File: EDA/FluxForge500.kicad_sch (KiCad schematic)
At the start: 0 parts

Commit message: Added more structure and added chosen power MOSFET
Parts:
- added Q1: SFG019N100C3, FluxForge500-lib:TO-247-4_L16.8-W5.0-L, symbol FluxForge500:SFG019N100C3
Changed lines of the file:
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@@
 	(generator_version "9.0")
 	(paper "A4")
+	(symbol
+		(lib_id "FluxForge500:SFG019N100C3")
+		(at 123.19 69.85 0)
+		(unit 1)
+		(exclude_from_sim no)
+		(in_bom yes)
+		(on_board yes)
+		(dnp no)
+		(fields_autoplaced yes)
+		(property "Reference" "Q1"
+			(at 130.81 69.8499 0)
+			(effects
+				(font
+					(size 1.27 1.27)
+				)
+				(justify left)
+			)
+		)
+		(property "Value" "SFG019N100C3"
+			(at 130.81 72.3899 0)
+			(effects
+				(font
+					(size 1.27 1.27)
+				)
+				(justify left)
+			)
+		)
+		(property "Footprint" "FluxForge500-lib:TO-247-4_L16.8-W5.0-L"
+			(at 123.19 82.55 0)
+			(effects
+				(font
+					(size 1.27 1.27)
+				)
+				(hide yes)
+			)
+		)
+		(property "Datasheet" "https://www.lcsc.com/datasheet/C49257109.pdf"
+			(at 123.19 85.09 0)
+			(effects
+				(font
+					(size 1.27 1.27)
+				)
+				(hide yes)
+			)
+		)
+		(property "Description" ""
+			(at 123.19 69.85 0)
+			(effects
+				(font
+					(size 1.27 1.27)
+				)
+				(hide yes)
+			)
+		)
+		(property "Manufacturer" "赛力康电气"
+			(at 123.19 87.63 0)
+			(effects
+				(font
+					(size 1.27 1.27)
+				)
+				(hide yes)
+			)
+		)
+		(property "MPN" "SFG019N100C3"
+			(at 123.19 90.17 0)
+			(effects
+				(font
+					(size 1.27 1.27)
+				)
+				(hide yes)
+			)
+		)
+		(property "LCSC Part" "C49257109"
+			(at 123.19 92.71 0)
+			(effects
+				(font
+					(size 1.27 1.27)
+				)
+				(hide yes)
+			)
+		)
+		(pin "3"
+		)
+		(pin "2"
+		)
+		(pin "1"
+		)
+		(pin "4"
+		)
+		(instances
+			(project ""
+				(path "/a2f35304-c637-43ce-ab88-fc8f2dc2eb48"
+					(reference "Q1")
+					(unit 1)
+				)
+			)
+		)
+	)
 	(sheet_instances
 		(path "/"

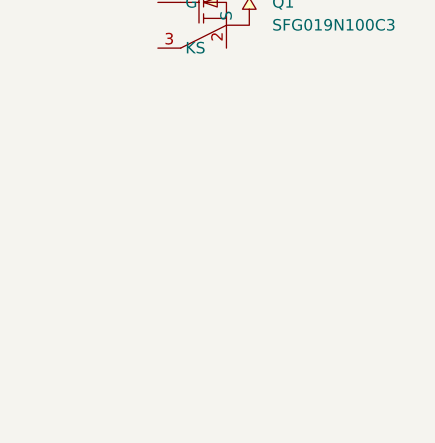
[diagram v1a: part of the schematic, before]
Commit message: Added chosen gate driver
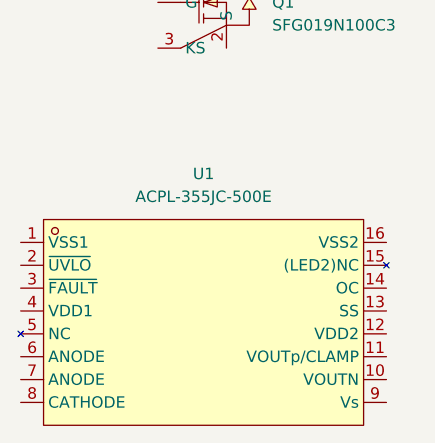
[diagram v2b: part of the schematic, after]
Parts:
- added U1: ACPL-355JC-500E, FluxForge500-lib:WSOIC-16_L10.3-W7.5-P1.27-LS10.3-BL, symbol FluxForge500:ACPL-355JC-500E
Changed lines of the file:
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@@
+		)
+	)
+	(symbol
+		(lib_id "FluxForge500:ACPL-355JC-500E")
+		(at 123.19 105.41 0)
+		(unit 1)
+		(exclude_from_sim no)
+		(in_bom yes)
+		(on_board yes)
+		(dnp no)
+		(fields_autoplaced yes)
+		(property "Reference" "U1"
+			(at 123.19 88.9 0)
+			(effects
+				(font
+					(size 1.27 1.27)
+				)
+			)
+		)
+		(property "Value" "ACPL-355JC-500E"
+			(at 123.19 91.44 0)
+			(effects
+				(font
+					(size 1.27 1.27)
+				)
+			)
+		)
+		(property "Footprint" "FluxForge500-lib:WSOIC-16_L10.3-W7.5-P1.27-LS10.3-BL"
+			(at 123.19 121.92 0)
+			(effects
+				(font
+					(size 1.27 1.27)
+				)
+				(hide yes)
+			)
+		)
+		(property "Datasheet" "https://www.lcsc.com/datasheet/C38013275.pdf"
+			(at 123.19 124.46 0)
+			(effects
+				(font
+					(size 1.27 1.27)
+				)
+				(hide yes)
+			)
+		)
+		(property "Description" ""
+			(at 123.19 105.41 0)
+			(effects
+				(font
+					(size 1.27 1.27)
+				)
+				(hide yes)
+			)
+		)
+		(property "Manufacturer" "Broadcom(博通)"
+			(at 123.19 127 0)
+			(effects
+				(font
+					(size 1.27 1.27)
+				)
+				(hide yes)
+			)
+		)
+		(property "MPN" "ACPL-355JC-500E"
+			(at 123.19 129.54 0)
+			(effects
+				(font
+					(size 1.27 1.27)
+				)
+				(hide yes)
+			)
+		)
+		(property "LCSC Part" "C38013275"
+			(at 123.19 132.08 0)
+			(effects
+				(font
+					(size 1.27 1.27)
+				)
+				(hide yes)
+			)
+		)
+		(pin "8"
+		)
+		(pin "6"
+		)
+		(pin "4"
+		)
+		(pin "13"
+		)
+		(pin "2"
+		)
+		(pin "3"
+		)
+		(pin "5"
+		)
+		(pin "7"
+		)
+		(pin "1"
+		)
+		(pin "16"
+		)
+		(pin "15"
+		)
+		(pin "14"
+		)
+		(pin "11"
+		)
+		(pin "10"
+		)
+		(pin "12"
+		)
+		(pin "9"
+		)
+		(instances
+			(project ""
+				(path "/a2f35304-c637-43ce-ab88-fc8f2dc2eb48"
+					(reference "U1")
+					(unit 1)
+				)
+			)
 		)
 	)

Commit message: Worked on schematic
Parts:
- removed U1: ACPL-355JC-500E, FluxForge500-lib:WSOIC-16_L10.3-W7.5-P1.27-LS10.3-BL, symbol FluxForge500:ACPL-355JC-500E
- added C1: 47pF, symbol Device:C
- added C10, C11, C7, C8, C9: 10uF, symbol Device:C
- added C12, C13: 180uF, symbol Device:C
- added C14: 1uF, symbol Device:C
- added C2, C3, C4, C5, C6: 4.7uF, symbol Device:C
- added L1: L, symbol Device:L
- added Q2, Q3, Q4: SFG019N100C3, FluxForge500-lib:TO-247-4_L16.8-W5.0-L, symbol FluxForge500:SFG019N100C3
- added R1, R2, R3, R4: 10Ω, symbol Device:R
- added R10, R6, R7, R9: 100Ω, symbol Device:R
- added R5: 8mΩ, symbol Device:R
- added R8: 0Ω, symbol Device:R
- added U1, U2, U3, U4: STGAP2SCMTR, FluxForge500-lib:SO-8_L4.9-W3.9-P1.27-LS5.9-BL, symbol FluxForge500:STGAP2SMTR
- added U5: LM5176PWPR, FluxForge500-lib:HTSSOP-28_L9.7-W4.4-P0.65-LS6.4-BL-EP, symbol FluxForge500:LM5176PWPR
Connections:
- net at Q1.1 (D): now also C2.1, C3.1, C4.1, C5.1, C6.1
- net at Q1.2 (S): now also L1.1, Q2.1 (D)
- net at Q1.3 (KS): now also U1.8 (GNDISO)
- net at Q1.4 (G): now also R1.2, U1.7 (CLAMP)
- new net: Q2.2 (S), Q4.2 (S), R5.1, R6.2
- new net: Q2.3 (KS), U2.8 (GNDISO)
- new net: Q2.4 (G), R2.2, U2.7 (CLAMP)
- new net: Q3.4 (G), R3.1, U3.7 (CLAMP)
- new net: R3.2, U3.6 (GOUT)
- new net: C10.1, C11.1, C7.1, C8.1, C9.1, Q3.1 (D), R10.2, R8.1
- new net: R1.1, U1.6 (GOUT)
- new net: R2.1, U2.6 (GOUT)
- new net: L1.2, Q3.2 (S), Q4.1 (D)
- new net: Q4.4 (G), R4.1, U4.7 (CLAMP)
- new net: R4.2, U4.6 (GOUT)
- new net: Q3.3 (KS), U3.8 (GNDISO)
- new net: C12.2, C13.2
- new net: Q4.3 (KS), U4.8 (GNDISO)
- new net CS: C1.1, R6.1, U5.16 (CS)
- new net CSG: C1.2, R7.1, U5.15 (CSG)
- new net GND: C10.2, C11.2, C2.2, C3.2, C4.2, C5.2, C6.2, C7.2, C8.2, C9.2, R5.2, R7.2
- new net HDRV1: U1.2 (IN+), U2.3 (IN-), U5.27 (HDRV1)
- new net HDRV2: U5.19 (HDRV2)
- new net ISNS+: C14.2, R10.1, U5.14 (ISNS(+))
- new net ISNS-: C14.1, R9.1, U5.13 (ISNS(-))
- new net LDRV1: U1.3 (IN-), U2.2 (IN+), U5.25 (LDRV1)
- new net LDRV2: U5.21 (LDRV2)
- new net VOUT: C12.1, C13.1, R8.2, R9.2
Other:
- note added: "Notes: R1, 2, 3, and 4 can be brought down to 4,7Ω experimentally. Recalculate Cin and Cout."
- moved on the sheet: Q1

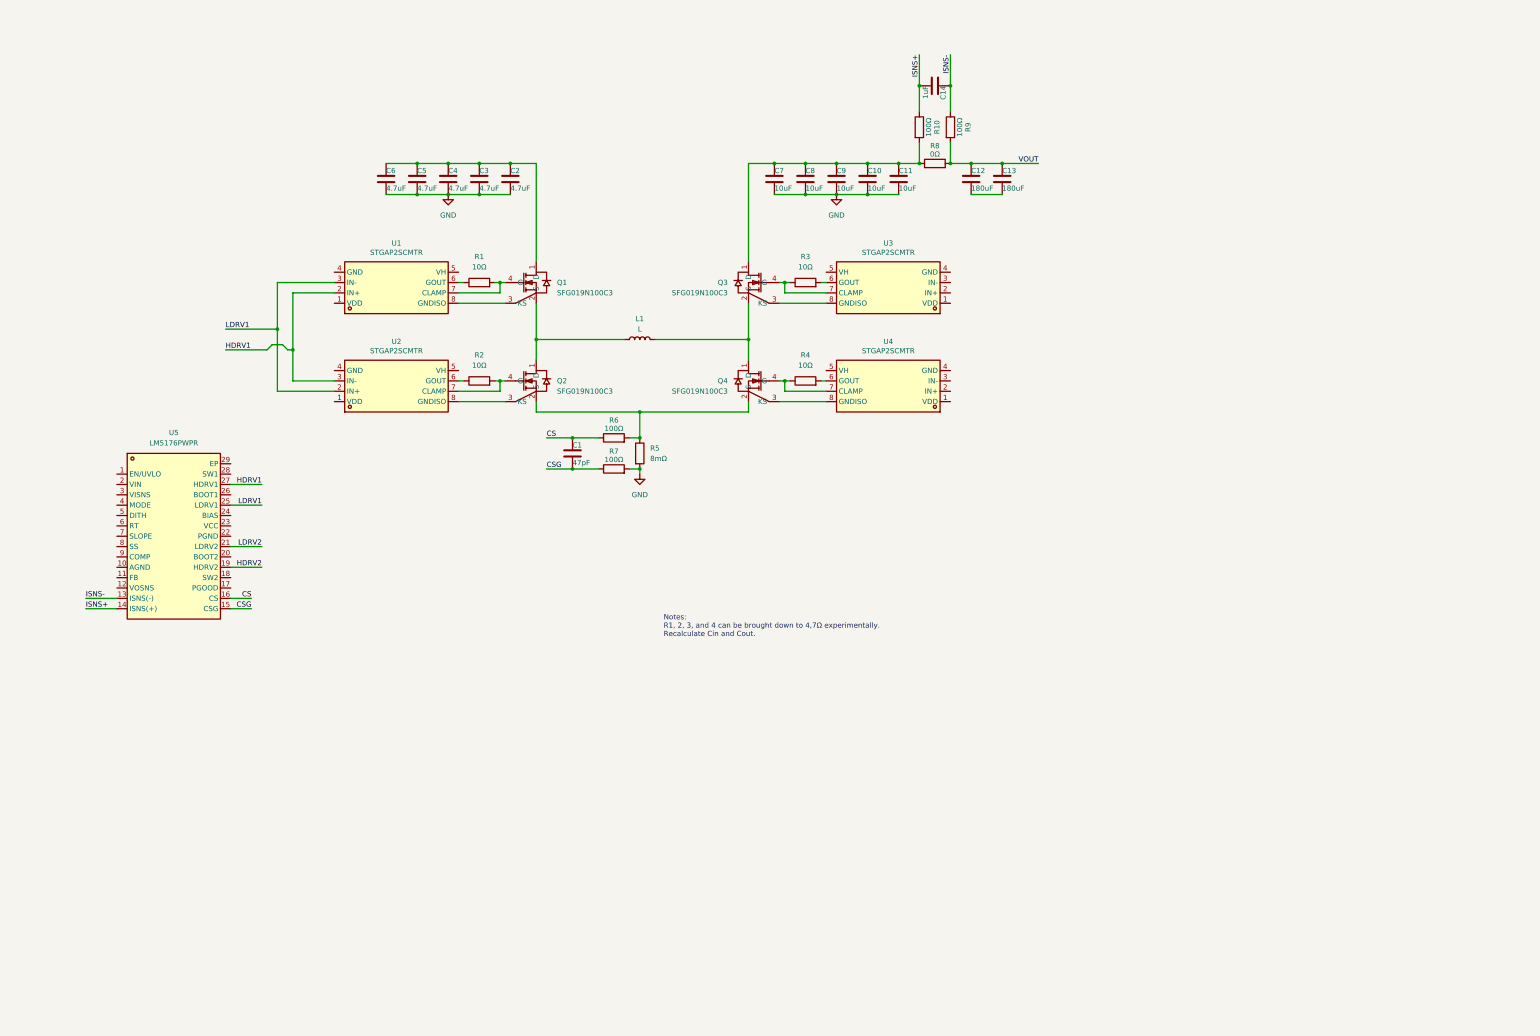
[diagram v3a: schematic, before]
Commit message: Uploaded work, added Octave file for calculating characteristics.
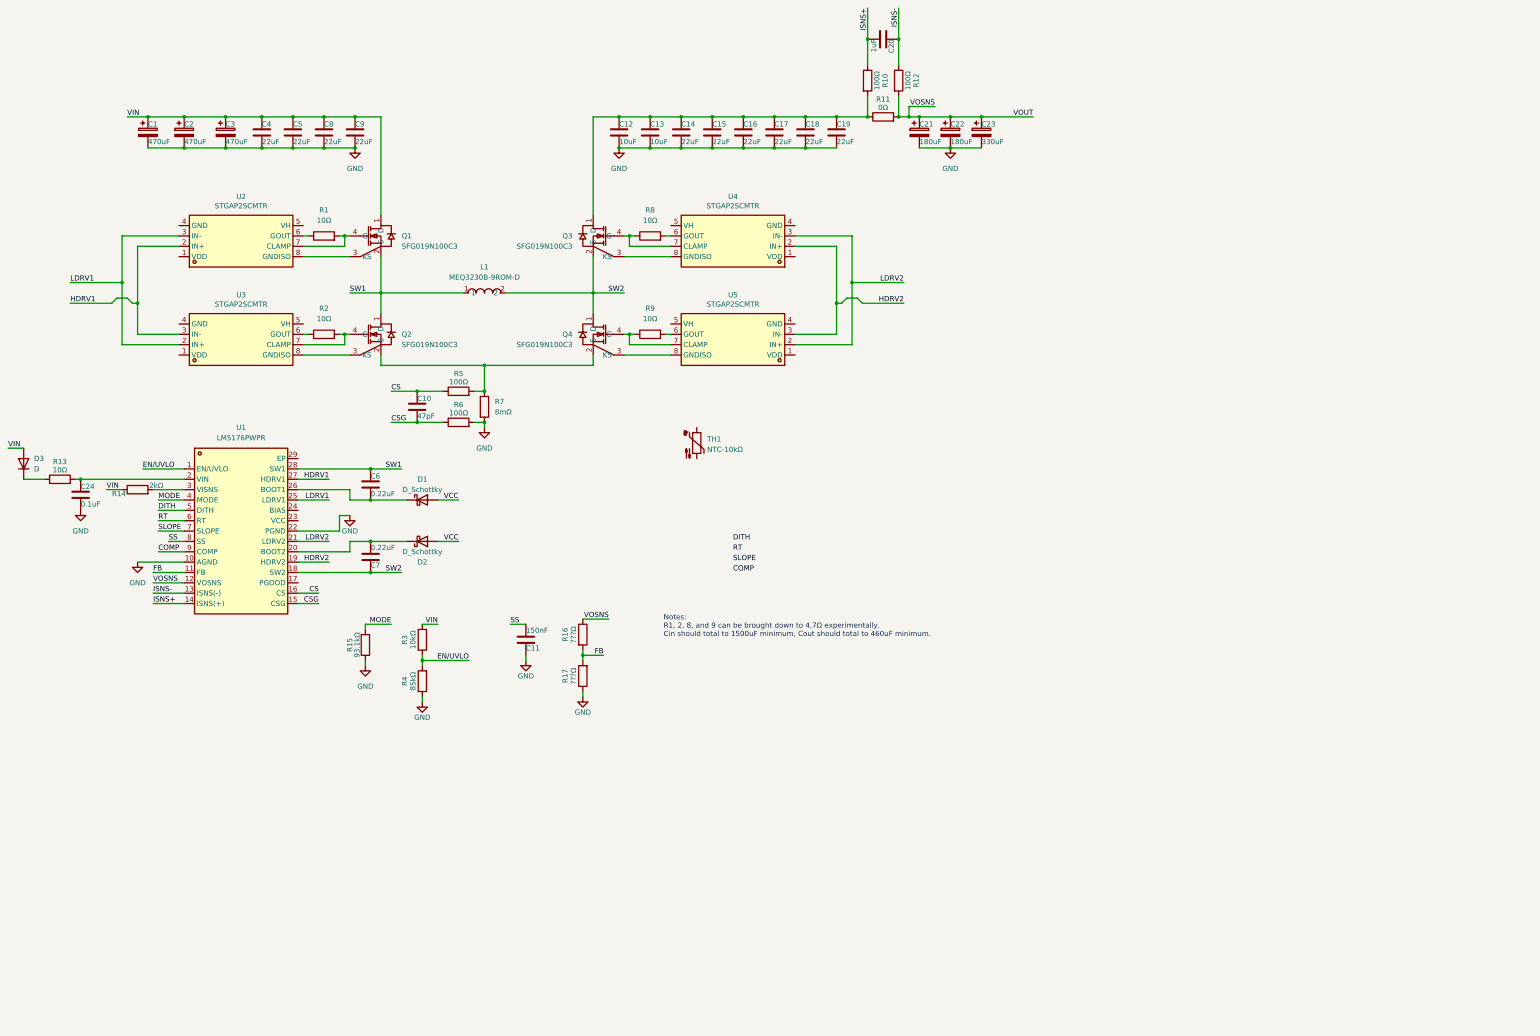
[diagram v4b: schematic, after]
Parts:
- removed L1: L, symbol Device:L
- added C1, C2, C3: 470uF, Capacitor_THT:CP_Radial_D10.0mm_P5.00mm, symbol Device:C_Polarized
- added C11: 150nF, symbol Device:C
- added C19: 22uF, Capacitor_SMD:C_2220_5750Metric, symbol Device:C
- added C21, C22: 180uF, Capacitor_THT:CP_Radial_D10.0mm_P5.00mm, symbol Device:C_Polarized
- added C23: 330uF, Capacitor_THT:CP_Radial_D10.0mm_P5.00mm, symbol Device:C_Polarized
- added C24: 0.1uF, symbol Device:C
- added C7: 0.22uF, symbol Device:C
- added D1, D2: D_Schottky, symbol Device:D_Schottky
- added D3: D, symbol Device:D
- added L1: MEQ3230B-9ROM-D, FluxForge500-lib:IND-TH_MEQ3230B-9ROM-D, symbol FluxForge500:MEQ3230B-9ROM-D
- added R13: 10Ω, symbol Device:R
- added R14: 2kΩ, symbol Device:R
- added R15: 93.1kΩ, symbol Device:R
- added R16, R17: ???Ω, symbol Device:R
- added R3: 10kΩ, symbol Device:R
- added R4: 85kΩ, symbol Device:R
- added TH1: NTC-10kΩ, FluxForge500-lib:NTC-TH_L8.8-W5.5-P1.50-D0.2, symbol FluxForge500:Thermistor_NTC-NTCALUG03A103H
- C12, C13: value 180uF -> 10uF; footprint (none) -> Capacitor_SMD:C_1210_3225Metric; MPN (none) -> FS32X106K101EGG
- C14: renamed from C7; value 10uF -> 22uF; footprint (none) -> Capacitor_SMD:C_2220_5750Metric; MPN (none) -> FS55X226K101LRG
- C15: renamed from C8; value 10uF -> 22uF; footprint (none) -> Capacitor_SMD:C_2220_5750Metric; MPN (none) -> FS55X226K101LRG
- C16: renamed from C9; value 10uF -> 22uF; footprint (none) -> Capacitor_SMD:C_2220_5750Metric; MPN (none) -> FS55X226K101LRG
- C17: renamed from C10; value 10uF -> 22uF; footprint (none) -> Capacitor_SMD:C_2220_5750Metric; MPN (none) -> FS55X226K101LRG
- C18: renamed from C11; value 10uF -> 22uF; footprint (none) -> Capacitor_SMD:C_2220_5750Metric; MPN (none) -> FS55X226K101LRG
- C4: renamed from C5; value 4.7uF -> 22uF; footprint (none) -> Capacitor_SMD:C_2220_5750Metric; MPN (none) -> FS55X226K101LRG
- C5: renamed from C4; value 4.7uF -> 22uF; footprint (none) -> Capacitor_SMD:C_2220_5750Metric; MPN (none) -> FS55X226K101LRG
- C6: value 4.7uF -> 0.22uF
- C8: renamed from C3; value 4.7uF -> 22uF; footprint (none) -> Capacitor_SMD:C_2220_5750Metric; MPN (none) -> FS55X226K101LRG
- C9: renamed from C2; value 4.7uF -> 22uF; footprint (none) -> Capacitor_SMD:C_2220_5750Metric; MPN (none) -> FS55X226K101LRG
- renumbered C1 to C10, C14 to C20, R8 to R11, R9 to R12, R6 to R5, R7 to R6, R5 to R7, R3 to R8, R4 to R9, U5 to U1, U1 to U2, U2 to U3, U3 to U4, U4 to U5
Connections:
- net GND: now also C12.2, C13.2, U1.10 (AGND), U1.22 (PGND), C1.2, C11.1, C19.2, C2.2, C21.2, C22.2, C23.2, C24.2, C3.2, R15.1, R17.1, R4.1; no longer C6.2
- net HDRV2: now also U4.2 (IN+), U5.3 (IN-)
- net LDRV2: now also U4.3 (IN-), U5.2 (IN+)
- net SW1: now reaches Q1.2 (S), Q2.1 (D)
- net SW1: now also C6.1, U1.28 (SW1), L1.1
- net VIN: now reaches C4.1, C5.1, C8.1, C9.1, Q1.1 (D)
- net VIN: now also C1.1, C2.1, C3.1, D3.2 (A), R14.1, R3.2; no longer C6.1
- net at C14.1, C15.1, C16.1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: now also C12.1, C13.1, C19.1
- net SW2: now reaches Q3.2 (S), Q4.1 (D)
- net SW2: now also U1.18 (SW2), C7.1, L1.2
- net EN/UVLO: now reaches U1.1 (EN/UVLO)
- net EN/UVLO: now also R3.1, R4.2
- net FB: now reaches U1.11 (FB)
- net FB: now also R16.2, R17.2
- net VOSNS: now reaches U1.12 (VOSNS)
- net VOSNS: now also R11.2, R12.2, C21.1, C22.1, C23.1, R16.1
- net at U1.2 (VIN): now also C24.1, R13.2
- net at U1.20 (BOOT2): now also C7.2, D2.1 (K)
- net at U1.26 (BOOT1): now also C6.2, D1.1 (K)
- net at U1.3 (VISNS): now also R14.2
- net MODE: now reaches U1.4 (MODE)
- net MODE: now also R15.2
- net DITH: now reaches U1.5 (DITH)
- net RT: now reaches U1.6 (RT)
- net SLOPE: now reaches U1.7 (SLOPE)
- net SS: now reaches U1.8 (SS)
- net SS: now also C11.2
- net COMP: now reaches U1.9 (COMP)
- removed net VOUT: C12.1, C13.1, R11.2, R12.2
- new net: D3.1 (K), R13.1
- new net VCC: D1.2 (A), D2.2 (A)
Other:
- note added: "Notes: R1, 2, 8, and 9 can be brought down to 4,7Ω experimentally. Cin should total to 1500uF minimum, Cout should total to 460uF minimum."
- note removed: "Notes: R1, 2, 3, and 4 can be brought down to 4,7Ω experimentally. Recalculate Cin and Cout."
- moved on the sheet: C10, C14, C15, C16, C17, C18, C20, C4, C5, C8, C9, Q1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
